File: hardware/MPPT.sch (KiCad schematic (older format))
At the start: 26 parts

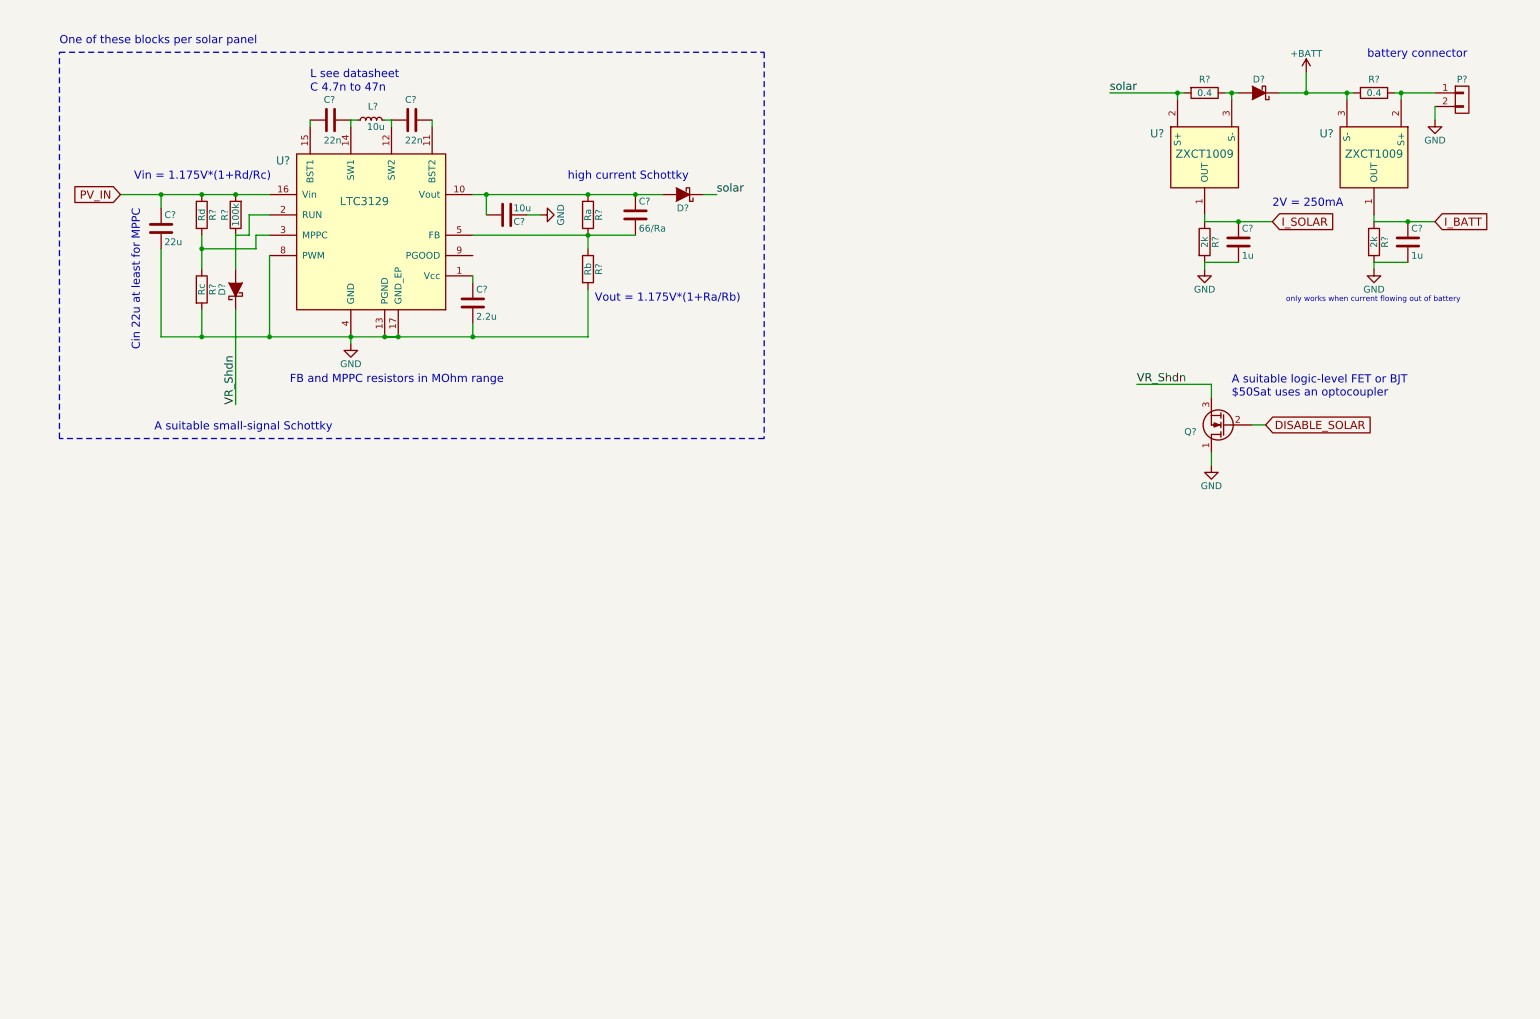
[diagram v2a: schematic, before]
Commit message: Updated MPPT
5 converter blocks, footprints and Digikey references for many components.
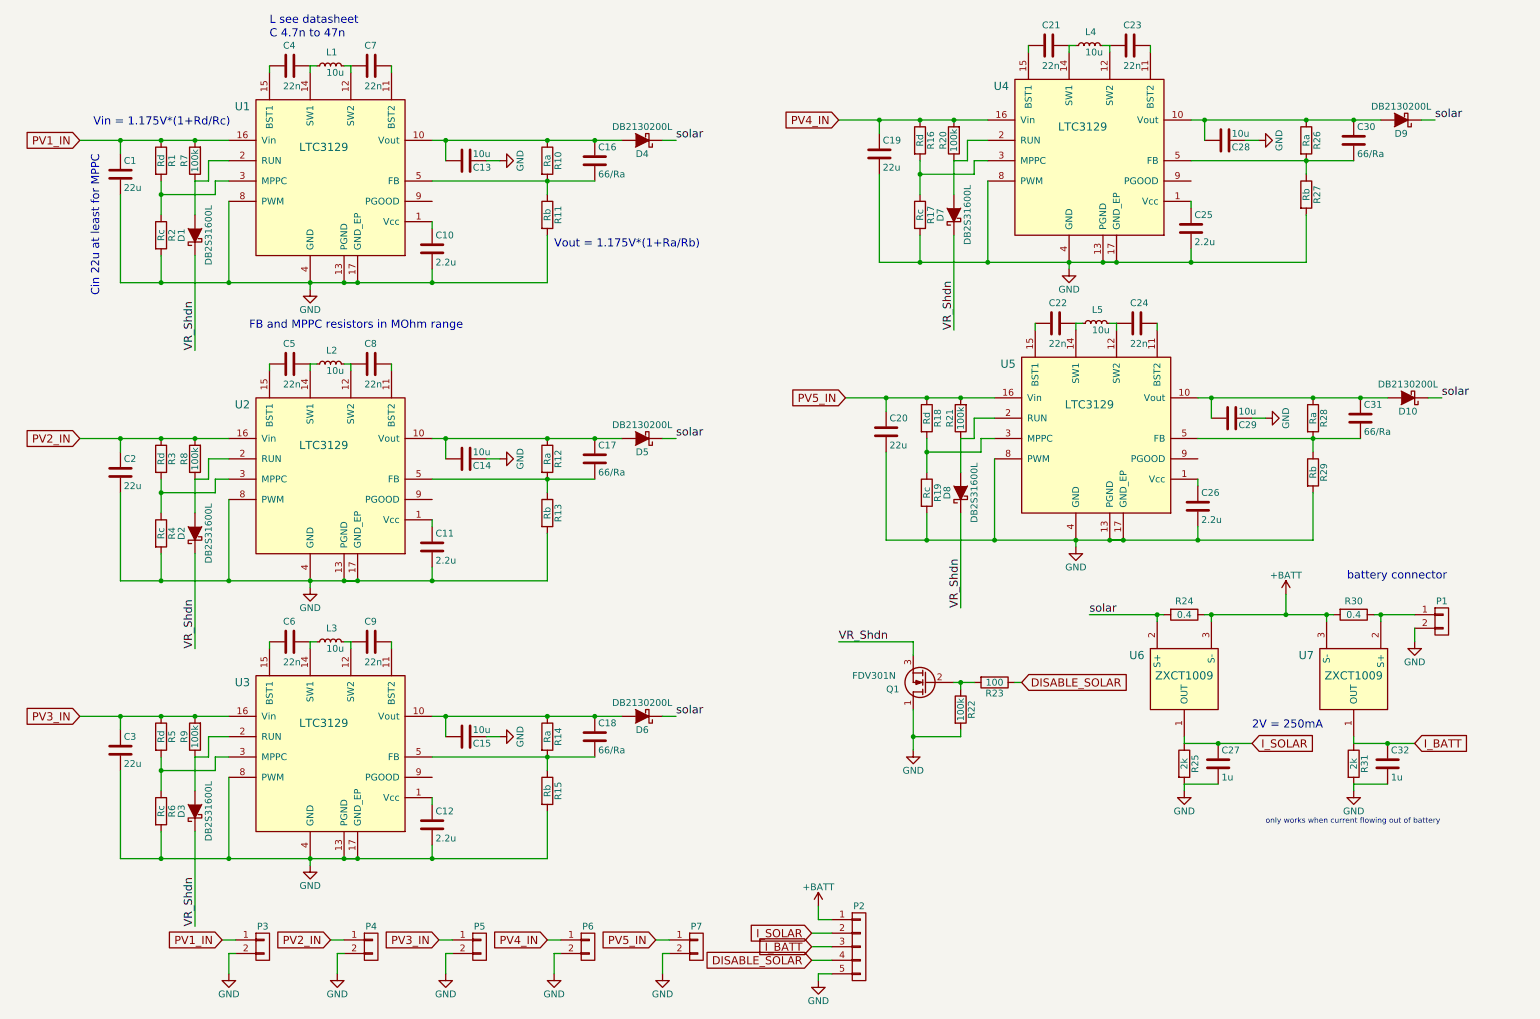
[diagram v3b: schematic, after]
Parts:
- removed D?: D_Schottky, symbol D_Schottky
- added C11, C12, C25, C26: 2.2u, Capacitors_SMD:C_0603, symbol C
- added C14, C15, C28, C29: 10u, Capacitors_SMD:C_0805, symbol C
- added C17, C18, C30, C31: 66/Ra, Capacitors_SMD:C_0603, symbol C
- added C19, C2, C20, C3: 22u, Capacitors_SMD:C_1210, symbol C
- added C21, C22, C23, C24, C5, C6, C8, C9: 22n, Capacitors_SMD:C_0603, symbol C
- added D10, D5, D6, D9: DB2130200L, symbol D_Schottky
- added D2, D3, D7, D8: DB2S31600L, Diodes_SMD:SOD-523, symbol D_Schottky
- added L2, L3, L4, L5: 10u, Capacitors_SMD:C_1210, symbol L_Small
- added P2: CONN_01X05, Pin_Headers:Pin_Header_Straight_1x05, symbol CONN_01X05
- added P3, P4, P5, P6, P7: CONN_01X02, Pin_Headers:Pin_Header_Straight_1x02, symbol CONN_01X02
- added R12, R14, R26, R28: Ra, Resistors_SMD:R_0603, symbol R
- added R13, R15, R27, R29: Rb, Resistors_SMD:R_0603, symbol R
- added R16, R18, R3, R5: Rd, Resistors_SMD:R_0603, symbol R
- added R17, R19, R4, R6: Rc, Resistors_SMD:R_0603, symbol R
- added R20, R21, R22, R8, R9: 100k, Resistors_SMD:R_0603, symbol R
- added R23: 100, Resistors_SMD:R_0603, symbol R
- added U2, U3, U4, U5: LTC3129, Housings_SSOP:MSOP-16-1EP-VIA_3x4mm_Pitch0.5mm, symbol LTC3129
- C1: renamed from C?; footprint (none) -> Capacitors_SMD:C_1210; Digikey (none) -> 1276-3395-1-ND
- C10: renamed from C?; footprint (none) -> Capacitors_SMD:C_0603; Digikey (none) -> 1276-2017-1-ND
- C13: renamed from C?; footprint (none) -> Capacitors_SMD:C_0805; Digikey (none) -> 1276-1113-1-ND
- C16, C4, C7: renamed from C?; footprint (none) -> Capacitors_SMD:C_0603
- C27, C32: renamed from C?; footprint (none) -> Capacitors_SMD:C_0603; Digikey (none) -> 1276-6524-1-ND
- D1: renamed from D?; value D_Schottky -> DB2S31600L; footprint (none) -> Diodes_SMD:SOD-523; Digikey (none) -> DB2S31600LCT-ND
- D4: renamed from D?; value D_Schottky -> DB2130200L; Digikey (none) -> DB2130200LCT-ND
- L1: renamed from L?; footprint (none) -> Capacitors_SMD:C_1210; Digikey (none) -> 490-5348-1-ND
- P1: renamed from P?; footprint (none) -> Pin_Headers:Pin_Header_Straight_1x02
- Q1: renamed from Q?; value Q_NMOS_DGS -> FDV301N; footprint (none) -> TO_SOT_Packages_SMD:SOT-23
- R1, R10, R11, R2, R25, R31, R7: renamed from R?; footprint (none) -> Resistors_SMD:R_0603
- R24, R30: renamed from R?; footprint (none) -> Resistors_SMD:R_1206; Digikey (none) -> 311-.4LWCT-ND
- U1: renamed from U?; footprint (none) -> Housings_SSOP:MSOP-16-1EP-VIA_3x4mm_Pitch0.5mm
- U6, U7: renamed from U?; footprint (none) -> TO_SOT_Packages_SMD:SOT-23
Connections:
- net +BATT: now also R24.1, U6.3 (S-), P2.1 (P1)
- net DISABLE_SOLAR: now also P2.4 (P4), R23.1; no longer Q1.2 (G)
- net GND: now also C11.2, C12.2, C14.1, C15.1, C19.2, C2.2, C20.2, C25.2, C26.2, C28.1, C29.1, C3.2, P2.5 (P5), P3.2 (P2), P4.2 (P2), P5.2 (P2), P6.2 (P2), P7.2 (P2), R13.2, R15.2, R17.2, R19.2, R22.2, R27.2, R29.2, R4.2, R6.2, U2.13 (PGND), U2.17 (GND_EP), U2.4 (GND), U2.8 (PWM), U3.13 (PGND), U3.17 (GND_EP), U3.4 (GND), U3.8 (PWM), U4.13 (PGND), U4.17 (GND_EP), U4.4 (GND), U4.8 (PWM), U5.13 (PGND), U5.17 (GND_EP), U5.4 (GND), U5.8 (PWM)
- net I_BATT: now also P2.3 (P3)
- net I_SOLAR: now also P2.2 (P2)
- net VR_Shdn: now also D2.1 (K), D3.1 (K), D7.1 (K), D8.1 (K)
- net solar: now also D10.1 (K), D5.1 (K), D6.1 (K), D9.1 (K)
- net PV_IN renamed PV1_IN
- net PV1_IN: now also P3.1 (P1)
- new net: Q1.2 (G), R22.1, R23.2
- new net: C11.1, U2.1 (Vcc)
- new net: C14.2, C17.1, D5.2 (A), R12.1, U2.10 (Vout)
- new net: C8.1, U2.11 (BST2)
- new net: C8.2, L2.2, U2.12 (SW2)
- new net: C5.1, L2.1, U2.14 (SW1)
- new net: C5.2, U2.15 (BST1)
- new net: D2.2 (A), R8.1, U2.2 (RUN)
- new net: R3.2, R4.1, U2.3 (MPPC)
- new net: C17.2, R12.2, R13.1, U2.5 (FB)
- new net: C25.1, U4.1 (Vcc)
- new net: C28.2, C30.1, D9.2 (A), R26.1, U4.10 (Vout)
- new net: C23.1, U4.11 (BST2)
- new net: C23.2, L4.2, U4.12 (SW2)
- new net: C21.1, L4.1, U4.14 (SW1)
- new net: C21.2, U4.15 (BST1)
- new net: D7.2 (A), R20.1, U4.2 (RUN)
- new net: R16.2, R17.1, U4.3 (MPPC)
- new net: C30.2, R26.2, R27.1, U4.5 (FB)
- new net: C26.1, U5.1 (Vcc)
- new net: C29.2, C31.1, D10.2 (A), R28.1, U5.10 (Vout)
- new net: C24.1, U5.11 (BST2)
- new net: C24.2, L5.2, U5.12 (SW2)
- new net: C22.1, L5.1, U5.14 (SW1)
- new net: C22.2, U5.15 (BST1)
- new net: D8.2 (A), R21.1, U5.2 (RUN)
- new net: R18.2, R19.1, U5.3 (MPPC)
- new net: C31.2, R28.2, R29.1, U5.5 (FB)
- new net: C12.1, U3.1 (Vcc)
- new net: C15.2, C18.1, D6.2 (A), R14.1, U3.10 (Vout)
- new net: C9.1, U3.11 (BST2)
- new net: C9.2, L3.2, U3.12 (SW2)
- new net: C6.1, L3.1, U3.14 (SW1)
- new net: C6.2, U3.15 (BST1)
- new net: D3.2 (A), R9.1, U3.2 (RUN)
- new net: R5.2, R6.1, U3.3 (MPPC)
- new net: C18.2, R14.2, R15.1, U3.5 (FB)
- new net PV2_IN: C2.1, P4.1 (P1), R3.1, R8.2, U2.16 (Vin)
- new net PV3_IN: C3.1, P5.1 (P1), R5.1, R9.2, U3.16 (Vin)
- new net PV4_IN: C19.1, P6.1 (P1), R16.1, R20.2, U4.16 (Vin)
- new net PV5_IN: C20.1, P7.1 (P1), R18.1, R21.2, U5.16 (Vin)
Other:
- note removed: "A suitable logic-level FET or BJT\n$50Sat uses an optocoupler"
- note removed: "A suitable small-signal Schottky"
- note removed: "One of these blocks per solar panel"
- note removed: "high current Schottky"
- moved on the sheet: C1, C10, C13, C16, C27, C32, C4, C7, D1, D4, L1, P1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

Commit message: Added SMini2 footprint
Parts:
- D10, D4, D5, D6, D9: footprint (none) -> smini:SMini2-F4-B-B
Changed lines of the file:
@@
 F 0 "D4" H 5000 1500 50  0000 C CNN
 F 1 "DB2130200L" H 5000 1300 50  0000 C CNN
-F 2 "" H 5000 1400 60  0001 C CNN
+F 2 "smini:SMini2-F4-B-B" H 5000 1400 60  0001 C CNN
 F 3 "" H 5000 1400 60  0000 C CNN
 F 4 "DB2130200LCT-ND" H 5000 1400 60  0001 C CNN "Digikey"
@@
 F 0 "D5" H 5000 3700 50  0000 C CNN
 F 1 "DB2130200L" H 5000 3500 50  0000 C CNN
-F 2 "" H 5000 3600 60  0001 C CNN
+F 2 "smini:SMini2-F4-B-B" H 5000 3600 60  0001 C CNN
 F 3 "" H 5000 3600 60  0000 C CNN
 F 4 "DB2130200LCT-ND" H 5000 3600 60  0001 C CNN "Digikey"
@@
 F 0 "D9" H 10600 1350 50  0000 C CNN
 F 1 "DB2130200L" H 10600 1150 50  0000 C CNN
-F 2 "" H 10600 1250 60  0001 C CNN
+F 2 "smini:SMini2-F4-B-B" H 10600 1250 60  0001 C CNN
 F 3 "" H 10600 1250 60  0000 C CNN
 F 4 "DB2130200LCT-ND" H 10600 1250 60  0001 C CNN "Digikey"
@@
 F 0 "D10" H 10650 3400 50  0000 C CNN
 F 1 "DB2130200L" H 10650 3200 50  0000 C CNN
-F 2 "" H 10650 3300 60  0001 C CNN
+F 2 "smini:SMini2-F4-B-B" H 10650 3300 60  0001 C CNN
 F 3 "" H 10650 3300 60  0000 C CNN
 F 4 "DB2130200LCT-ND" H 10650 3300 60  0001 C CNN "Digikey"
@@
 F 0 "D6" H 5000 5750 50  0000 C CNN
 F 1 "DB2130200L" H 5000 5550 50  0000 C CNN
-F 2 "" H 5000 5650 60  0001 C CNN
+F 2 "smini:SMini2-F4-B-B" H 5000 5650 60  0001 C CNN
 F 3 "" H 5000 5650 60  0000 C CNN
 F 4 "DB2130200LCT-ND" H 5000 5650 60  0001 C CNN "Digikey"
